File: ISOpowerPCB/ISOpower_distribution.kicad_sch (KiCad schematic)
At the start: 30 parts, among them M1 Fan_IEC60617, Q2 IRF5305_PBF, Q3 IRF5305_PBF, U10 LM2596S-5, U11 74HC02, U4 i6A4W020A-DC-DC-250W, U5 i6A4W020A-DC-DC-250W, U6 ACS712xLCTR-30A, U7 ACS712xLCTR-30A, U8 74HC02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

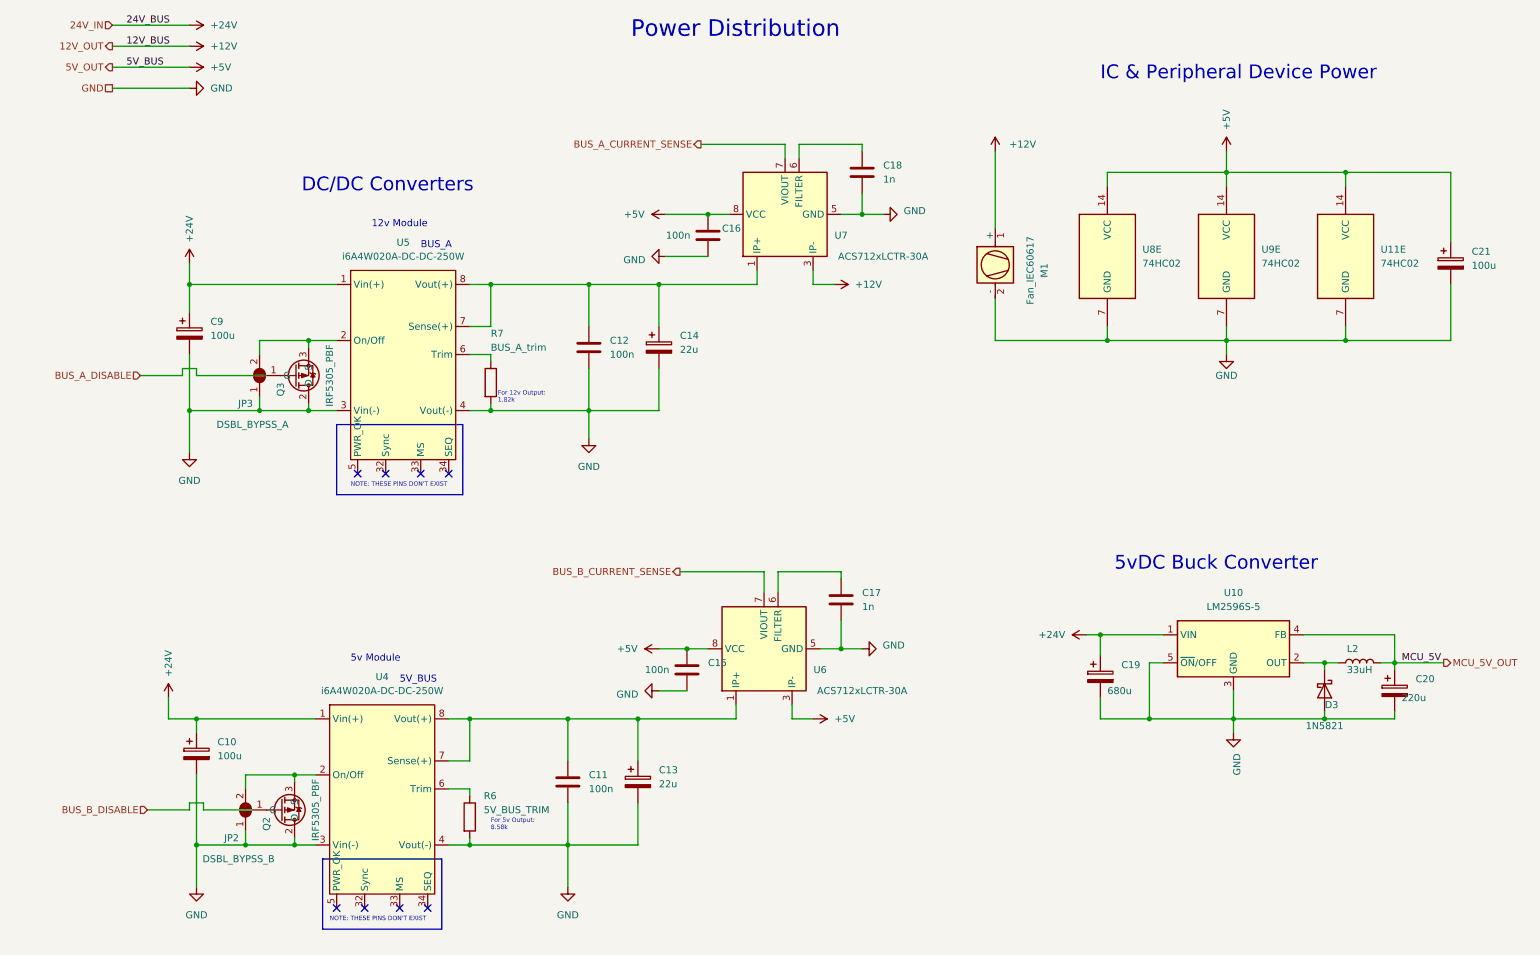
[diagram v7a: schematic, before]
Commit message: fixed most electrical rules check violations
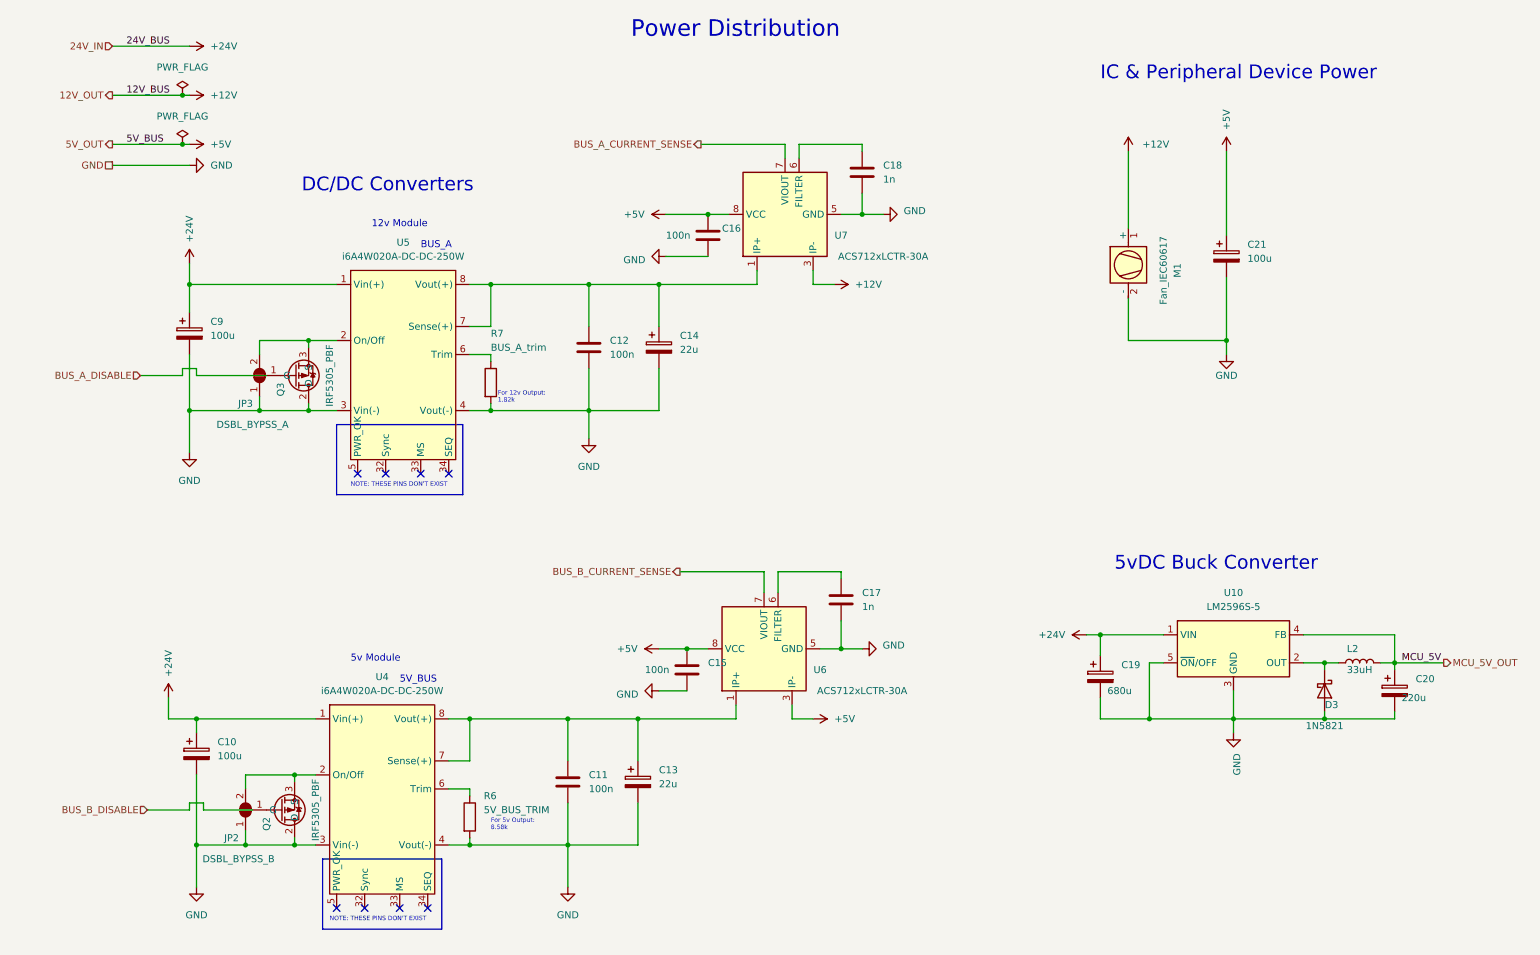
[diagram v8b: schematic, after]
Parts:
- removed U11, U8, U9: 74HC02, symbol 74xx:74HC02
- C11, C12, C15, C16, C17, C18: symbol 000_Capacitor_FIlm_Immo:cap_film_0805 -> 000_Capacitor_Film_Immo:cap_film_0805
- C19: symbol 000_Capacitor_Electrolytic_Immo:680u -> 000_Capacitor_Electrolytic_Immo:100u
- C20: symbol 000_Capacitor_Electrolytic_Immo:220u -> 000_Capacitor_Electrolytic_Immo:100u
- M1: symbol 009_Heat_Management_Immo:Fan_IEC60617 -> 000_Heat_Management_Immo:Fan_IEC60617
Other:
- moved on the sheet: C21, M1
